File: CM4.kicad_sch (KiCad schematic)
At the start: 11 parts, among them J11 Conn_01x02, J12 Conn_01x02, J16 Conn_02x05_Odd_Even, J6 Conn_01x02, J7 HDMI_A_2.0, U1 RaspberryPi-CM4Lite, U2 DF40C-100DS-0.4V(51), U3 DF40C-100DS-0.4V(51)

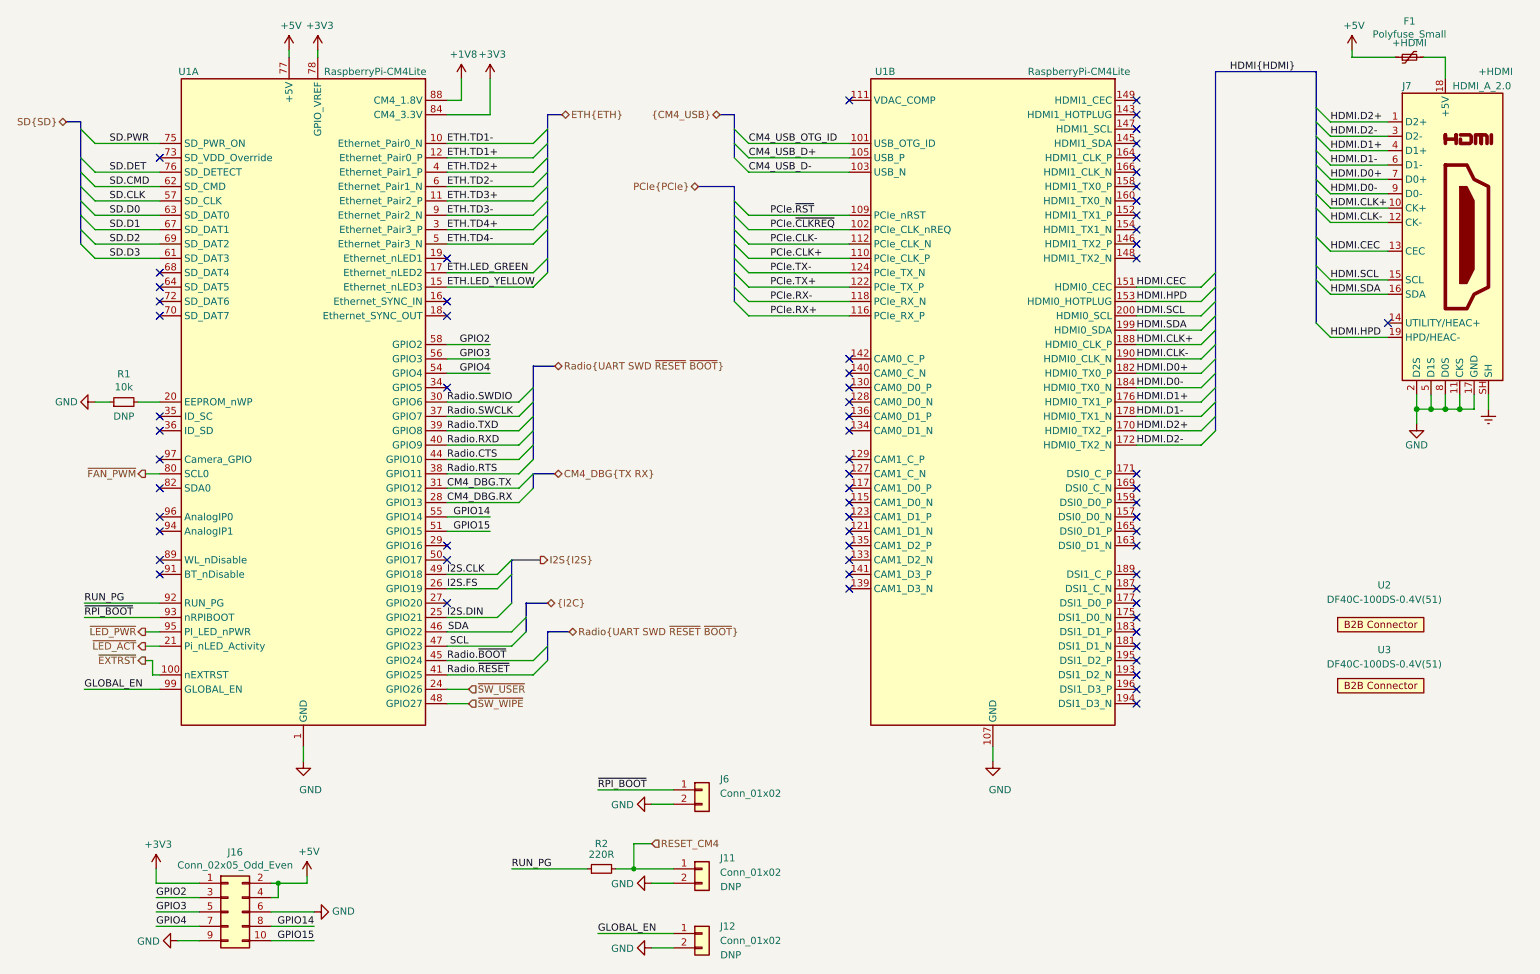
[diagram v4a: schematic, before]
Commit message: Update silkscreen/adjust reference designators
Order some relevant reference designator. Use JP for all jumpers. Place
silkcreen neatly. Add some custom silk screen. Remove heat sink corner
marks on silk screen.

Signed-off-by: Stefan Agner <stefan@agner.ch>
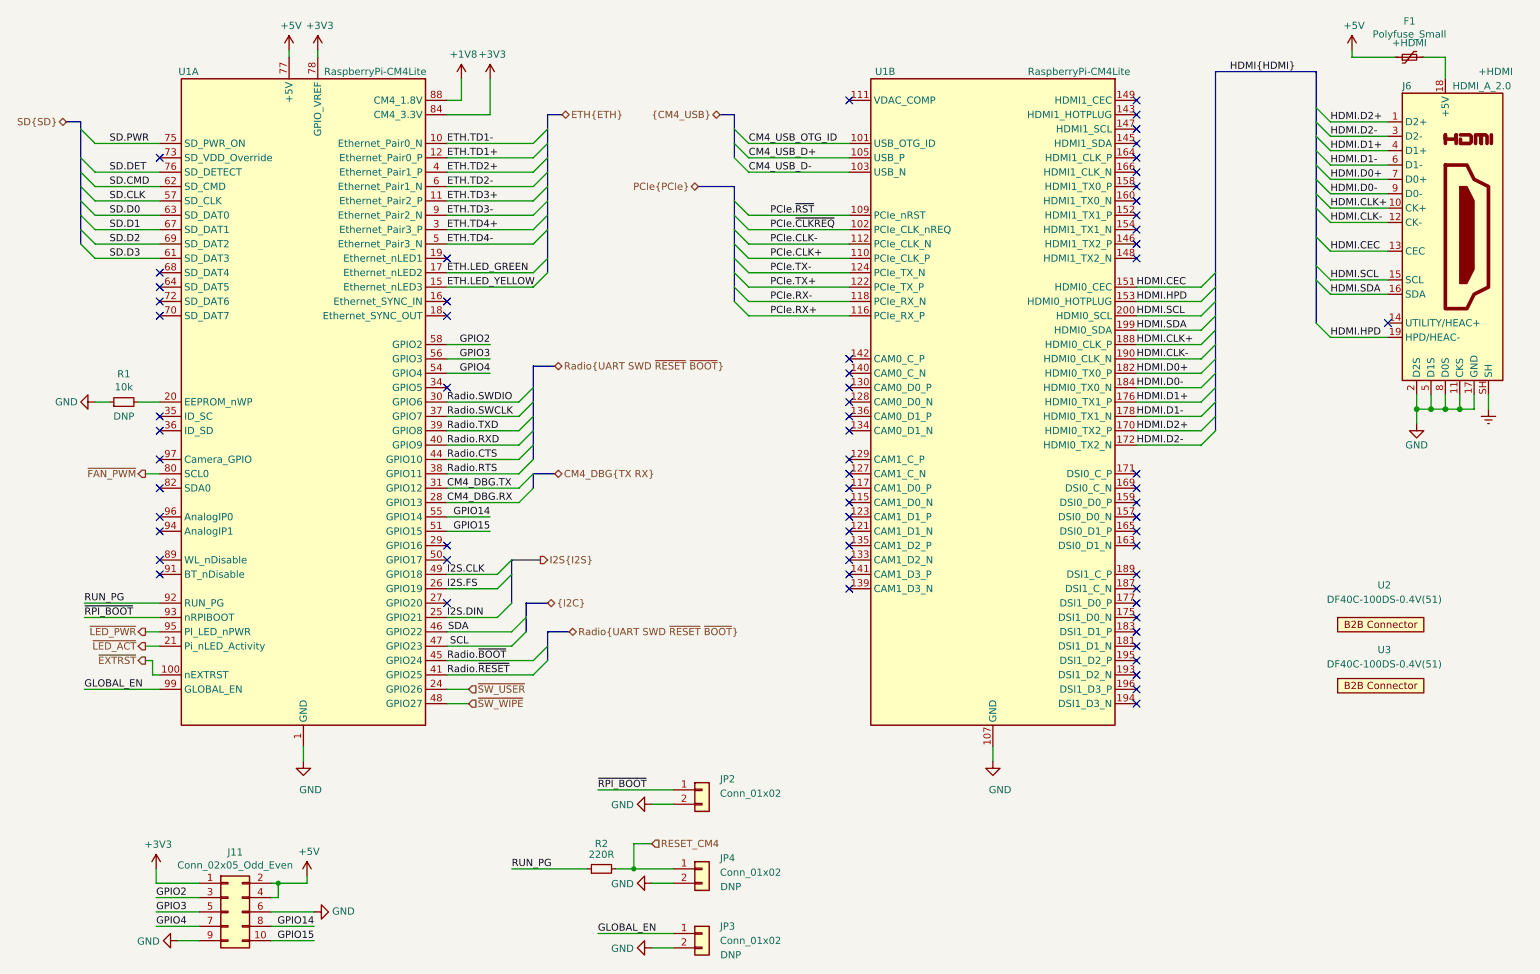
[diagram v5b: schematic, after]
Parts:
- renumbered J16 to J11, J7 to J6, J6 to JP2, J12 to JP3, J11 to JP4
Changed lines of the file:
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@@
     (comment 2 "Light Blue")
   )
+  (bus_alias "HDMI" (members "D0+" "D0-" "D1+" "D1-" "D2+" "D2-" "CLK+" "CLK-" "CEC" "HPD" "SDA" "SCL"))
+  (bus_alias "UART" (members "TXD" "RXD" "CTS" "RTS"))
+  (bus_alias "SD" (members "D[0..3]" "CMD" "CLK" "PWR" "DET"))
   (bus_alias "PCIe" (members "~RST" "~CLKREQ" "CLK+" "CLK-" "TX+" "TX-" "RX+" "RX-"))
-  (bus_alias "SD" (members "D[0..3]" "CMD" "CLK" "PWR" "DET"))
-  (bus_alias "UART" (members "TXD" "RXD" "CTS" "RTS"))
-  (bus_alias "HDMI" (members "D0+" "D0-" "D1+" "D1-" "D2+" "D2-" "CLK+" "CLK-" "CEC" "HPD" "SDA" "SCL"))
   (junction (at 59.055 173.99) (diameter 0.9144) (color 0 0 0 0))
   (junction (at 121.92 171.45) (diameter 0.9144) (color 0 0 0 0))
@@
   (symbol (lib_id "Connector_Generic:Conn_01x02") (at 133.985 157.48 0) (unit 1)
     (in_bom yes) (on_board yes)
-    (property "Reference" "J6" (id 0) (at 137.16 155.5749 0)
+    (property "Reference" "JP2" (id 0) (at 137.16 155.5749 0)
       (effects (font (size 1.27 1.27)) (justify left))
     )
@@
   (symbol (lib_id "Connector_Generic:Conn_01x02") (at 133.985 171.45 0) (unit 1)
     (in_bom yes) (on_board yes)
-    (property "Reference" "J11" (id 0) (at 137.16 169.5449 0)
+    (property "Reference" "JP4" (id 0) (at 137.16 169.5449 0)
       (effects (font (size 1.27 1.27)) (justify left))
     )
@@
   (symbol (lib_id "Connector_Generic:Conn_01x02") (at 133.985 182.88 0) (unit 1)
     (in_bom yes) (on_board yes)
-    (property "Reference" "J12" (id 0) (at 137.16 181.6099 0)
+    (property "Reference" "JP3" (id 0) (at 137.16 181.6099 0)
       (effects (font (size 1.27 1.27)) (justify left))
     )
@@
   (symbol (lib_id "Connector_Generic:Conn_02x05_Odd_Even") (at 50.165 179.07 0) (unit 1)
     (in_bom yes) (on_board yes)
-    (property "Reference" "J16" (id 0) (at 51.435 168.5098 0))
+    (property "Reference" "J11" (id 0) (at 51.435 168.5098 0))
     (property "Value" "Conn_02x05_Odd_Even" (id 1) (at 51.435 170.8085 0))
     (property "Footprint" "Connector_PinHeader_2.54mm:PinHeader_2x05_P2.54mm_Vertical" (id 2) (at 50.165 179.07 0)
@@
   (symbol (lib_id "Connector:HDMI_A_1.4") (at 265.43 59.69 0) (unit 1)
     (in_bom yes) (on_board yes)
-    (property "Reference" "J7" (id 0) (at 257.81 33.02 0)
+    (property "Reference" "J6" (id 0) (at 257.81 33.02 0)
       (effects (font (size 1.27 1.27)) (justify left))
     )

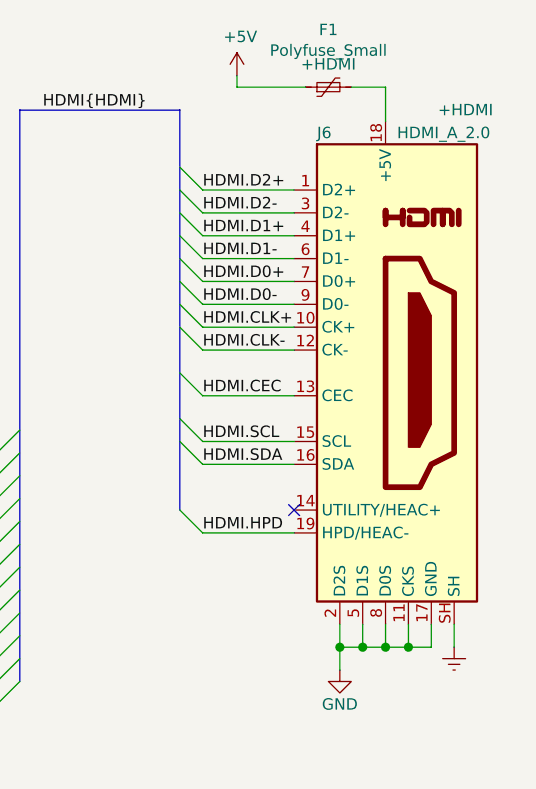
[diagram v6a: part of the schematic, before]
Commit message: Use HDMI Type D (mini HDMI) Symbol
This fixes assignment of pins to properly match HDMI Type D pinout.

Fixes: #24

Signed-off-by: Stefan Agner <stefan@agner.ch>
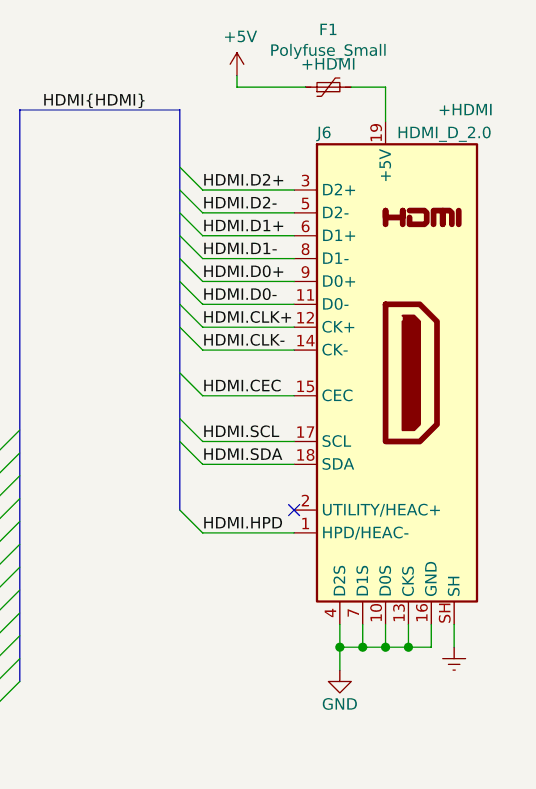
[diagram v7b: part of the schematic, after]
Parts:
- J6: value HDMI_A_2.0 -> HDMI_D_2.0; symbol Connector:HDMI_A_1.4 -> Connector:HDMI_D_1.4
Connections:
- net GND: now also J6.10 (D0S), J6.13 (CKS), J6.16 (GND), J6.4 (D2S), J6.7 (D1S); no longer J6.11 (CKS), J6.17 (GND), J6.2 (D2S), J6.5 (D1S), J6.8 (D0S)
- net HDMI.CEC: now also J6.15 (CEC); no longer J6.13 (CEC)
- net HDMI.CLK+: now also J6.12 (CK+); no longer J6.10 (CK+)
- net HDMI.CLK-: now also J6.14 (CK-); no longer J6.12 (CK-)
- net HDMI.D0+: now also J6.9 (D0+); no longer J6.7 (D0+)
- net HDMI.D0-: now also J6.11 (D0-); no longer J6.9 (D0-)
- net HDMI.D1+: now also J6.6 (D1+); no longer J6.4 (D1+)
- net HDMI.D1-: now also J6.8 (D1-); no longer J6.6 (D1-)
- net HDMI.D2+: now also J6.3 (D2+); no longer J6.1 (D2+)
- net HDMI.D2-: now also J6.5 (D2-); no longer J6.3 (D2-)
- net HDMI.HPD: now also J6.1 (HPD/HEAC-); no longer J6.19 (HPD/HEAC-)
- net HDMI.SCL: now also J6.17 (SCL); no longer J6.15 (SCL)
- net HDMI.SDA: now also J6.18 (SDA); no longer J6.16 (SDA)
- net at F1.2: now also J6.19 (+5V); no longer J6.18 (+5V)
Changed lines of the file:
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@@
     (pin "9")
   )
-  (symbol (lib_id "Connector:HDMI_A_1.4") (at 265.43 59.69 0) (unit 1)
+  (symbol (lib_id "Connector:HDMI_D_1.4") (at 265.43 59.69 0) (unit 1)
     (in_bom yes) (on_board yes)
     (property "Reference" "J6" (id 0) (at 257.81 33.02 0)
       (effects (font (size 1.27 1.27)) (justify left))
     )
-    (property "Value" "HDMI_A_2.0" (id 1) (at 266.7 33.02 0)
+    (property "Value" "HDMI_D_2.0" (id 1) (at 266.7 33.02 0)
       (effects (font (size 1.27 1.27)) (justify left))
     )
@@
       (effects (font (size 1.27 1.27)) hide)
     )
-    (property "Datasheet" "https://en.wikipedia.org/wiki/HDMI" (id 3) (at 266.065 59.69 0)
+    (property "Datasheet" "http://pinoutguide.com/PortableDevices/micro_hdmi_type_d_pinout.shtml" (id 3) (at 266.065 59.69 0)
       (effects (font (size 1.27 1.27)) hide)
     )
